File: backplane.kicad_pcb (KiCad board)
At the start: 4 copper layers, 110 x 90 mm, 57 parts, among them IC1 SiC437AED-T1-GE3, J1 46010-0622, J2 46010-0622, J4 212520-1006, J5 XT60PW-F

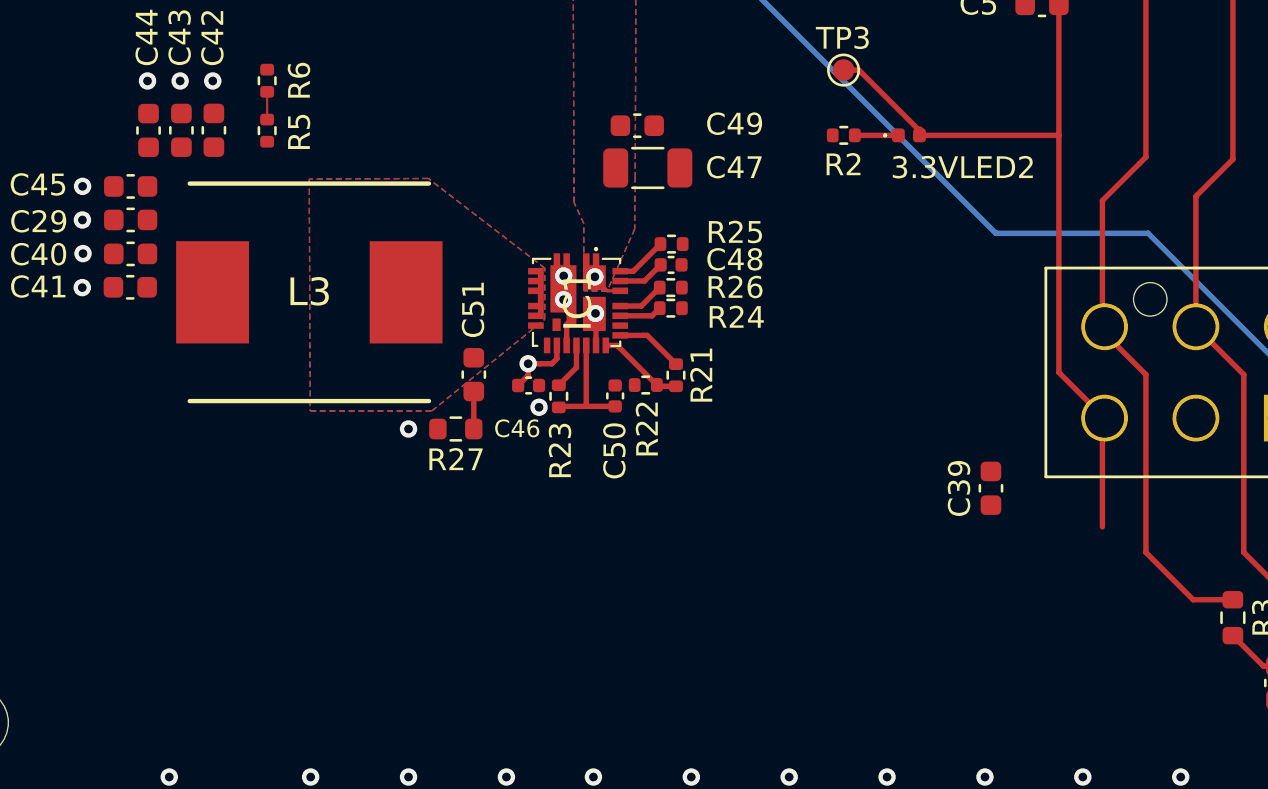
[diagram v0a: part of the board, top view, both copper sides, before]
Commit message: 10 more to go
DRC reduction
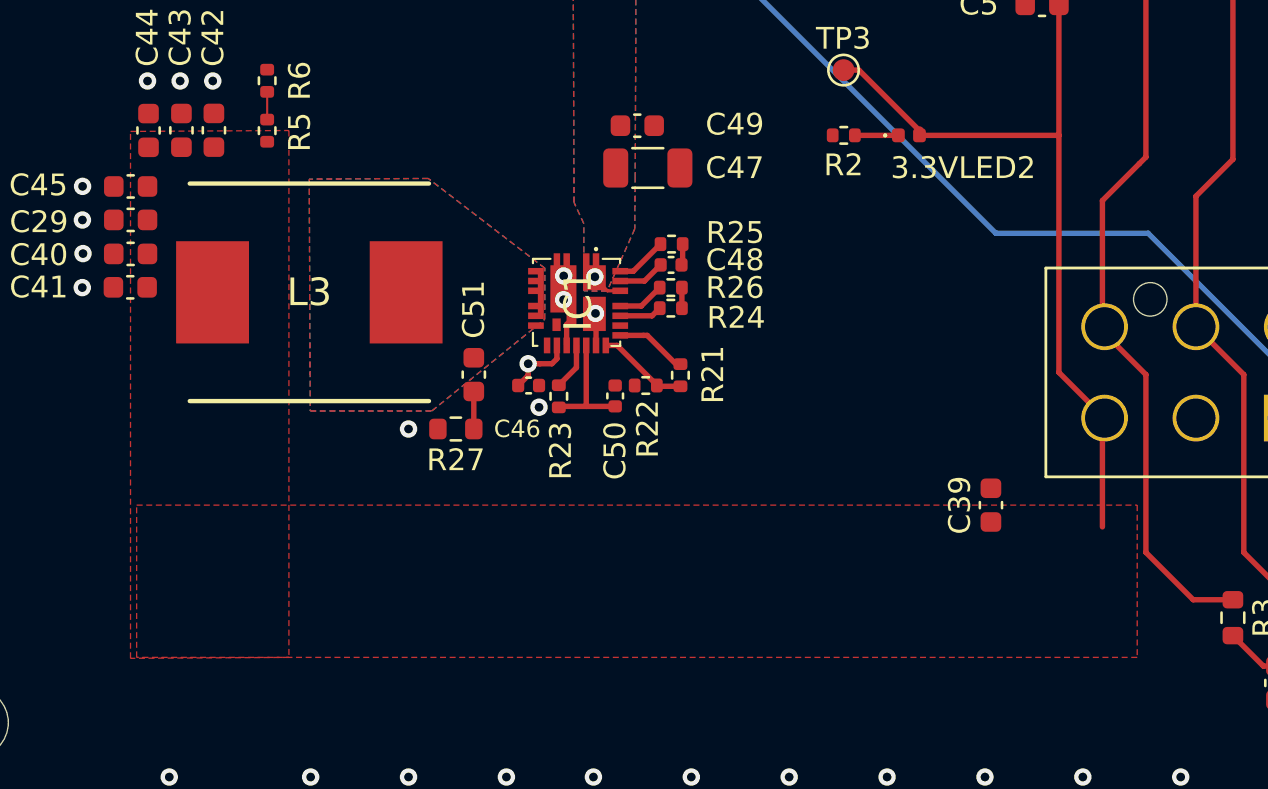
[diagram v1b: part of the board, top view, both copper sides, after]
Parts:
- moved C39 0.78 mm to (137.8, 134.0)
- moved R21 0.20 mm to (123.5, 128.0)
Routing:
- net Net-(C48-Pad2): track 0.00 -> 0.98 mm
- net /buckC/Vdd: track 5.41 -> 6.36 mm
- added copper zone on F.Cu, net RBUS_uC_V
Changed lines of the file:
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@@
 	(footprint "Resistor_SMD:R_0402_1005Metric"
 		(layer "F.Cu")
-		(at 121.905661 128.48 180)
+		(at 121.905661 128.5 180)
 		(descr "Resistor SMD 0402 (1005 Metric), square (rectangular) end terminal, IPC_7351 nominal, (Body size source: IPC-SM-782 page 72, https://www.pcb-3d.com/wordpress/wp-content/uploads/ipc-sm-782a_amendment_1_and_2.pdf), generated with kicad-footprint-generator")
 		(tags "resistor")
 		(property "Reference" "R22"
-			(at -0.094339 -2.02 90)
+			(at -0.094339 -2 90)
 			(layer "F.SilkS")
 			(effects
@@
 	(footprint "Capacitor_SMD:C_0603_1608Metric"
 		(layer "F.Cu")
-		(at 137.775 133.225 90)
+		(at 137.775 134 90)
 		(descr "Capacitor SMD 0603 (1608 Metric), square (rectangular) end terminal, IPC_7351 nominal, (Body size source: IPC-SM-782 page 76, https://www.pcb-3d.com/wordpress/wp-content/uploads/ipc-sm-782a_amendment_1_and_2.pdf), generated with kicad-footprint-generator")
 		(tags "capacitor")
@@
 	(footprint "Resistor_SMD:R_0402_1005Metric"
 		(layer "F.Cu")
-		(at 123.295094 128.027312 90)
+		(at 123.5 128.027312 90)
 		(descr "Resistor SMD 0402 (1005 Metric), square (rectangular) end terminal, IPC_7351 nominal, (Body size source: IPC-SM-782 page 72, https://www.pcb-3d.com/wordpress/wp-content/uploads/ipc-sm-782a_amendment_1_and_2.pdf), generated with kicad-footprint-generator")
 		(tags "resistor")
 		(property "Reference" "R21"
-			(at 0 1.204906 -90)
+			(at 0.027312 1.5 -90)
 			(layer "F.SilkS")
 			(effects
@@
 	)
 	(segment
+		(start 123.602837 122)
+		(end 123.602837 122.902478)
+		(width 0.25)
+		(layer "F.Cu")
+		(net 7)
+	)
+	(segment
+		(start 123.602837 122.902478)
+		(end 123.54975 122.955565)
+		(width 0.25)
+		(layer "F.Cu")
+		(net 7)
+	)
+	(segment
 		(start 119.169962 129.459173)
 		(end 119.170789 129.46)
@@
 	)
 	(segment
+		(start 123.567962 124.943322)
+		(end 123.568944 124.944304)
+		(width 0.25)
+		(layer "F.Cu")
+		(net 9)
+	)
+	(segment
 		(start 119.170789 129.46)
 		(end 117.955511 129.46)
@@
 	)
 	(segment
+		(start 123.567962 124)
+		(end 123.567962 124.943322)
+		(width 0.25)
+		(layer "F.Cu")
+		(net 9)
+	)
+	(segment
 		(start 119.169962 126.658561)
 		(end 119.169962 129.459173)
@@
 	)
 	(zone
-		(net 0)
-		(net_name "")
+		(net 22)
+		(net_name "RBUS_uC_V")
 		(layer "F.Cu")
 		(hatch edge 0.5)
+		(priority 3)
 		(connect_pads
 			(clearance 0)
@@
 		(min_thickness 0.25)
 		(filled_areas_thickness no)
-		(keepout
-			(tracks not_allowed)
-			(vias not_allowed)
-			(pads not_allowed)
-			(copperpour allowed)
-			(footprints allowed)
-		)
-		(fill
+		(fill yes
 			(thermal_gap 0.5)
 			(thermal_bridge_width 0.5)
@@
 		(polygon
 			(pts
-				(xy 106 116.84998) (xy 98.293282 116.84998) (xy 98.244014 139.193289) (xy 105.9541 139.189812)
+				(xy 144.5 134) (xy 144.5 141) (xy 98.5 141) (xy 98.5 134)
 			)
 		)
 	)
 	(zone
-		(net 0)
-		(net_name "")
+		(net 22)
+		(net_name "RBUS_uC_V")
 		(layer "F.Cu")
 		(hatch edge 0.5)
+		(priority 3)
 		(connect_pads
 			(clearance 0)
@@
 		(min_thickness 0.25)
 		(filled_areas_thickness no)
-		(keepout
-			(tracks not_allowed)
-			(vias not_allowed)
-			(pads not_allowed)
-			(copperpour allowed)
-			(footprints allowed)
-		)
-		(fill
+		(fill yes
 			(thermal_gap 0.5)
 			(thermal_bridge_width 0.5)
@@
 		(polygon
 			(pts
-				(xy 143.851182 139.133011) (xy 143.851182 133.426293) (xy 98.754924 133.647059) (xy 98.758401 139.357145)
+				(xy 105.5 141) (xy 98.217857 141.042101) (xy 98.217857 116.819394) (xy 105.5 116.777293)
 			)
 		)
@@
 		(priority 1)
 		(connect_pads yes
-			(clearance 0.5)
+			(clearance 0.254)
 		)
-		(min_thickness 0.25)
+		(min_thickness 0.254)
 		(filled_areas_thickness no)
 		(fill yes

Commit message: more changes
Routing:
- net Net-(IC1-V_DRV): vias 1 -> 0
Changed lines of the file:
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@@
 		(tags "Connector")
 		(property "Reference" "J2"
-			(at 0 0 0)
+			(at 12.2 -5.5 0)
 			(layer "F.SilkS")
 			(effects
@@
 		(at 90.3 110.9 -90)
 		(property "Reference" "J5"
-			(at -9.5675 6.7 0)
+			(at -9.9 -0.7 0)
 			(layer "F.SilkS")
 			(effects
@@
 		(tags "Integrated Circuit")
 		(property "Reference" "IC1"
-			(at -0.078 -0.068 90)
+			(at -5.677561 2.725962 90)
 			(layer "F.SilkS")
 			(effects
@@
 		(tags "Inductor")
 		(property "Reference" "L3"
-			(at 0 0 0)
+			(at 6.059832 -6.716397 0)
 			(layer "F.SilkS")
 			(effects
@@
 		(tags "Connector")
 		(property "Reference" "J1"
-			(at 0 0 0)
+			(at 12.8 -5.5 0)
 			(layer "F.SilkS")
 			(effects
@@
 		(tags "Connector")
 		(property "Reference" "J4"
-			(at 0 0 0)
+			(at 13.1 -2 0)
 			(layer "F.SilkS")
 			(effects
@@
 		(net 2)
 	)
-	(via
-		(at 116.5 127.5)
-		(size 0.8)
-		(drill 0.4)
-		(layers "F.Cu" "B.Cu")
-		(net 2)
-	)
 	(segment
 		(start 119.564433 123.504084)
@@
 		(width 0.25)
 		(layer "F.Cu")
+		(net 22)
+	)
+	(segment
+		(start 123.517312 127.5)
+		(end 123.5 127.517312)
+		(width 0.25)
+		(layer "F.Cu")

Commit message: more drcs out
last error is naming convention - after will neaten everything up + add a switch then should be done
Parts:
- moved C51 0.78 mm to (114.0, 127.2)
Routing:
- net Net-(IC1-EN): track 1.59 -> 14.3 mm, vias 1 -> 0
- net /buckC/SW: track 0.00 -> 7.23 mm
- net CAN_L: track 81.2 -> 79.8 mm
- net Net-(C51-Pad2): track 1.72 -> 2.50 mm
- added copper zone on F.Cu, net +3.3V
- added copper zone on F.Cu, net /buckC/SW
- removed copper zone on In2.Cu, net +3.3V
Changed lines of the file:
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@@
 	(footprint "Capacitor_SMD:C_0603_1608Metric"
 		(layer "F.Cu")
-		(at 114 128 -90)
+		(at 114 127.225 -90)
 		(descr "Capacitor SMD 0603 (1608 Metric), square (rectangular) end terminal, IPC_7351 nominal, (Body size source: IPC-SM-782 page 76, https://www.pcb-3d.com/wordpress/wp-content/uploads/ipc-sm-782a_amendment_1_and_2.pdf), generated with kicad-footprint-generator")
 		(tags "capacitor")
@@
 	)
 	(segment
-		(start 117.819962 126.658561)
-		(end 117.819962 127.271061)
-		(width 0.25)
-		(layer "F.Cu")
-		(net 2)
-	)
-	(segment
 		(start 116.5 127.5)
 		(end 116.5 128.04)
@@
 	)
 	(segment
-		(start 117.04 127.5)
-		(end 117.04 127.5)
+		(start 117.819962 126.658561)
+		(end 117.819962 127.271061)
 		(width 0.25)
 		(layer "F.Cu")
@@
 	(segment
 		(start 117.591023 127.5)
-		(end 117.04 127.5)
+		(end 116.5 127.5)
 		(width 0.25)
 		(layer "F.Cu")
@@
 	)
 	(segment
-		(start 117.04 127.5)
-		(end 116.5 127.5)
+		(start 120.144962 124.146561)
+		(end 119.544962 123.546561)
 		(width 0.25)
 		(layer "F.Cu")
-		(net 2)
+		(net 3)
+	)
+	(segment
+		(start 120.731962 124.146561)
+		(end 120.144962 124.146561)
+		(width 0.25)
+		(layer "F.Cu")
+		(net 3)
+	)
+	(segment
+		(start 124.325 125.091816)
+		(end 124.325 121.725)
+		(width 0.25)
+		(layer "F.Cu")
+		(net 3)
+	)
+	(segment
+		(start 120.731962 125.746561)
+		(end 123.670255 125.746561)
+		(width 0.25)
+		(layer "F.Cu")
+		(net 3)
 	)
 	(segment
@@
 	)
 	(segment
-		(start 120.144962 124.146561)
-		(end 119.564433 123.566032)
-		(width 0.15)
+		(start 121.1 118.5)
+		(end 120.525 118.5)
+		(width 0.25)
 		(layer "F.Cu")
 		(net 3)
 	)
 	(segment
-		(start 120.731962 124.146561)
-		(end 120.144962 124.146561)
-		(width 0.15)
+		(start 124.325 121.725)
+		(end 121.1 118.5)
+		(width 0.25)
+		(layer "F.Cu")
+		(net 3)
+	)
+	(segment
+		(start 120.525 116.773008)
+		(end 120.742267 116.555741)
+		(width 0.25)
+		(layer "F.Cu")
+		(net 3)
+	)
+	(segment
+		(start 123.670255 125.746561)
+		(end 124.325 125.091816)
+		(width 0.25)
 		(layer "F.Cu")
 		(net 3)
@@
 		(net 3)
 	)
-	(via
-		(at 119.564433 123.504084)
-		(size 0.8)
-		(drill 0.4)
-		(layers "F.Cu" "B.Cu")
-		(net 3)
-	)
 	(segment
 		(start 151.4 75.5)
@@
 	)
 	(segment
+		(start 115.153439 125.296561)
+		(end 114 126.45)
+		(width 0.25)
+		(layer "F.Cu")
+		(net 8)
+	)
+	(segment
+		(start 116.719962 125.296561)
+		(end 115.153439 125.296561)
+		(width 0.25)
+		(layer "F.Cu")
+		(net 8)
+	)
+	(segment
+		(start 113.123771 126.45)
+		(end 110.890168 124.216397)
+		(width 0.25)
+		(layer "F.Cu")
+		(net 8)
+	)
+	(segment
+		(start 114 126.45)
+		(end 113.123771 126.45)
+		(width 0.25)
+		(layer "F.Cu")
+		(net 8)
+	)
+	(segment
 		(start 119.169962 129.459173)
 		(end 119.170789 129.46)
@@
 	)
 	(segment
-		(start 114 128.775)
+		(start 114 128)
 		(end 114 130.5)
 		(width 0.25)
@@
 	)
 	(segment
+		(start 147.1 75.5)
+		(end 147.4 75.5)
+		(width 0.25)
+		(layer "F.Cu")
+		(net 20)
+	)
+	(segment
 		(start 147.1 65.925)
 		(end 147.1 75.5)
@@
 	)
 	(segment
-		(start 147.4 75.5)
-		(end 148.9 77)
-		(width 0.25)
-		(layer "F.Cu")
-		(net 20)
-	)
-	(segment
 		(start 147 98.5)
 		(end 148.9 100.4)
@@
 	)
 	(segment
-		(start 147.1 75.5)
-		(end 147.4 75.5)
-		(width 0.25)
-		(layer "F.Cu")
-		(net 20)
-	)
-	(segment
 		(start 148.9 100.4)
 		(end 148.9 118.1)
@@
 	)
 	(segment
+		(start 147.4 75.5)
+		(end 148.9 77)
+		(width 0.25)
+		(layer "F.Cu")
+		(net 20)
+	)
+	(segment
 		(start 151.535 138.31)
 		(end 153 138.31)
@@
 	)
 	(segment
-		(start 147.4 75.5)
-		(end 148.4 76.5)
-		(width 0.25)
-		(layer "F.Cu")
-		(net 20)
-	)
-	(segment
 		(start 147.2 125.8)
 		(end 149.4 128)
@@
 	)
 	(segment
-		(start 121.974343 126.196561)
-		(end 123.295094 127.517312)
-		(width 0.25)
-		(layer "F.Cu")
-		(net 22)
-	)
-	(segment
-		(start 121.803439 126.196561)
-		(end 120.731962 126.196561)
+		(start 123.517312 127.5)
+		(end 123.5 127.517312)
 		(width 0.25)
 		(layer "F.Cu")
@@
 	)
 	(segment
-		(start 121.803439 126.196561)
-		(end 121.974343 126.196561)
+		(start 122.179249 126.196561)
+		(end 123.5 127.517312)
 		(width 0.25)
 		(layer "F.Cu")
@@
 	)
 	(segment
-		(start 123.517312 127.5)
-		(end 123.5 127.517312)
+		(start 120.731962 126.196561)
+		(end 122.179249 126.196561)
 		(width 0.25)
 		(layer "F.Cu")
@@
 	)
 	(zone
-		(net 22)
-		(net_name "RBUS_uC_V")
+		(net 5)
+		(net_name "+3.3V")
 		(layer "F.Cu")
 		(hatch edge 0.5)
 		(priority 3)
-		(connect_pads
-			(clearance 0)
+		(connect_pads yes
+			(clearance 0.254)
 		)
-		(min_thickness 0.25)
+		(min_thickness 0.254)
 		(filled_areas_thickness no)
 		(fill yes
@@
 		(polygon
 			(pts
-				(xy 144.5 134) (xy 144.5 141) (xy 98.5 141) (xy 98.5 134)
+				(xy 144.5 134) (xy 144.5 141) (xy 98.257399 141.062453) (xy 98.250355 134.062411)
 			)
 		)
 	)
 	(zone
-		(net 22)
-		(net_name "RBUS_uC_V")
+		(net 8)
+		(net_name "/buckC/SW")
 		(layer "F.Cu")
 		(hatch edge 0.5)
-		(priority 3)
-		(connect_pads
-			(clearance 0)
+		(connect_pads yes
+			(clearance 0.254)
 		)
-		(min_thickness 0.25)
+		(min_thickness 0.254)
 		(filled_areas_thickness no)
 		(fill yes
-			(thermal_gap 0.5)
-			(thermal_bridge_width 0.5)
+			(thermal_gap 0.508)
+			(thermal_bridge_width 0.508)
 		)
 		(polygon
 			(pts
-				(xy 105.5 141) (xy 98.217857 141.042101) (xy 98.217857 116.819394) (xy 105.5 116.777293)
+				(xy 117.376946 122.576908) (xy 117.371423 126.001241) (xy 106.5 130) (xy 106.5 117.5)
 			)
 		)
 	)
 	(zone
-		(net 1)
-		(net_name "GND")
-		(layers "F.Cu" "In1.Cu" "B.Cu")
+		(net 22)
+		(net_name "RBUS_uC_V")
+		(layer "F.Cu")
 		(hatch edge 0.5)
-		(priority 1)
-		(connect_pads yes
+		(priority 3)
+		(connect_pads
 			(clearance 0.254)
 		)
@@
 		(polygon
 			(pts
-				(xy 207 149) (xy 207 55) (xy 86 55) (xy 86 149)
+				(xy 105.546351 141.025374) (xy 98.264208 141.067475) (xy 98.217857 116.819394) (xy 105.5 116.777293)
 			)
 		)
 	)
 	(zone
-		(net 4)
-		(net_name "+12V")
-		(layers "F&B.Cu")
+		(net 1)
+		(net_name "GND")
+		(layers "F.Cu" "In1.Cu" "B.Cu")
 		(hatch edge 0.5)
+		(priority 1)
 		(connect_pads yes
-			(clearance 0.254)
+			(clearance 0)
 		)
 		(min_thickness 0.25)
@@
 		(polygon
 			(pts
-				(xy 117.27 123.11) (xy 111.905051 118.981734) (xy 106.435051 119.011734) (xy 106.48 129.67) (xy 112.07 129.67)
-				(xy 117.26 125.46)
+				(xy 201.5 149) (xy 201.5 55) (xy 80.5 55) (xy 80.5 149)
 			)
 		)
@@
 			(clearance 0.254)
 		)
-		(min_thickness 0.25)
+		(min_thickness 0.254)
 		(filled_areas_thickness no)
 		(fill yes
@@
 			)
 		)
-	)
-	(zone
-		(net 1)
-		(net_name "GND")
-		(layer "In1.Cu")
-		(hatch edge 0.5)
-		(priority 2)
-		(connect_pads
-			(clearance 0.5)
-		)
-		(min_thickness 0.25)
-		(filled_areas_thickness no)
-		(fill yes
-			(thermal_gap 0.5)
-			(thermal_bridge_width 0.5)
-		)
-		(polygon
-			(pts
-				(xy 207 149) (xy 86 149) (xy 86 55) (xy 207 55)
-			)
-		)
-	)
-	(zone
-		(net 5)
-		(net_name "+3.3V")
-		(layer "In2.Cu")
-		(hatch edge 0.5)
-		(priority 1)
-		(connect_pads yes
-			(clearance 0.5)
-		)
-		(min_thickness 0.25)
-		(filled_areas_thickness no)
-		(fill yes
-			(thermal_gap 0.5)
-			(thermal_bridge_width 0.5)
-		)
-		(polygon
-			(pts
-				(xy 207 149) (xy 86 149) (xy 86 55) (xy 207 55) (xy 207 148)
-			)
-		)
-	)
-	(zone
-		(net 1)
-		(net_name "GND")
-		(layer "B.Cu")
-		(hatch edge 0.5)
-		(priority 4)
-		(connect_pads
-			(clearance 0.5)
-		)
-		(min_thickness 0.25)
-		(filled_areas_thickness no)
-		(fill yes
-			(thermal_gap 0.5)
-			(thermal_bridge_width 0.5)
-		)
-		(polygon
-			(pts
-				(xy 207 150) (xy 86 149) (xy 86 55) (xy 207 55)
-			)
-		)
